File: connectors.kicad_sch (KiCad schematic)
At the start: 4 parts, among them J1 Conn_01x04_Pin, J2 Conn_01x04_Pin, J3 Conn_01x09_Pin, J4 Conn_02x03_Odd_Even

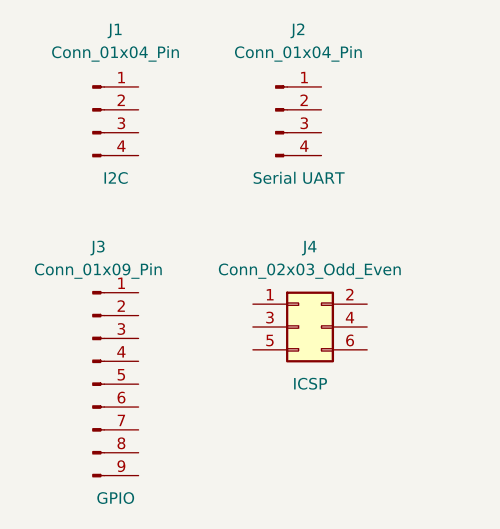
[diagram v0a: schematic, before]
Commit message: Arranged symbols.
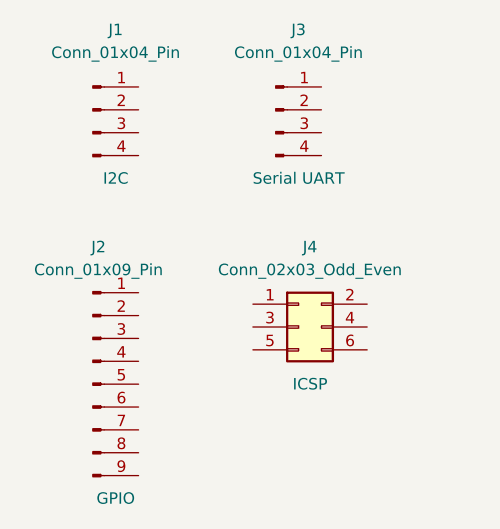
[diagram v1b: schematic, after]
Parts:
- renumbered J3 to J2, J2 to J3
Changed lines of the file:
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@@
 		(on_board yes)
 		(dnp no)
-		(property "Reference" "J3"
+		(property "Reference" "J2"
 			(at 93.345 87.63 0)
 			(effects
@@
 			(project ""
 				(path "/eb036d61-982e-41fc-ad07-0dff52d6a1cc/1c35631a-56f2-41a3-8845-0858340bff1a"
-					(reference "J3")
+					(reference "J2")
 					(unit 1)
 				)
@@
 		(on_board yes)
 		(dnp no)
-		(property "Reference" "J2"
+		(property "Reference" "J3"
 			(at 115.57 63.5 0)
 			(effects
@@
 			(project "MCU Datalogger"
 				(path "/eb036d61-982e-41fc-ad07-0dff52d6a1cc/1c35631a-56f2-41a3-8845-0858340bff1a"
-					(reference "J2")
+					(reference "J3")
 					(unit 1)
 				)

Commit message: Completed symbol-footprint associations.
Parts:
- J1, J3: footprint (none) -> Connector_PinHeader_2.54mm:PinHeader_1x04_P2.54mm_Vertical
- J2: footprint (none) -> Connector_PinHeader_2.54mm:PinHeader_1x09_P2.54mm_Vertical
- J4: footprint (none) -> Connector_PinHeader_2.54mm:PinHeader_2x03_P2.54mm_Vertical
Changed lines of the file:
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@@
 			)
 		)
-		(property "Footprint" ""
+		(property "Footprint" "Connector_PinHeader_2.54mm:PinHeader_2x03_P2.54mm_Vertical"
 			(at 115.57 96.52 0)
 			(effects
@@
 			)
 		)
-		(property "Footprint" ""
+		(property "Footprint" "Connector_PinHeader_2.54mm:PinHeader_1x09_P2.54mm_Vertical"
 			(at 92.71 102.87 0)
 			(effects
@@
 			)
 		)
-		(property "Footprint" ""
+		(property "Footprint" "Connector_PinHeader_2.54mm:PinHeader_1x04_P2.54mm_Vertical"
 			(at 113.03 72.39 0)
 			(effects
@@
 			)
 		)
-		(property "Footprint" ""
+		(property "Footprint" "Connector_PinHeader_2.54mm:PinHeader_1x04_P2.54mm_Vertical"
 			(at 92.71 72.39 0)
 			(effects

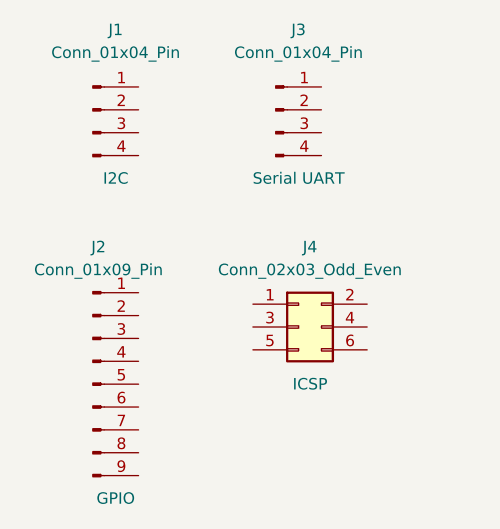
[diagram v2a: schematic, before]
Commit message: Completed wiring in the second sheet.
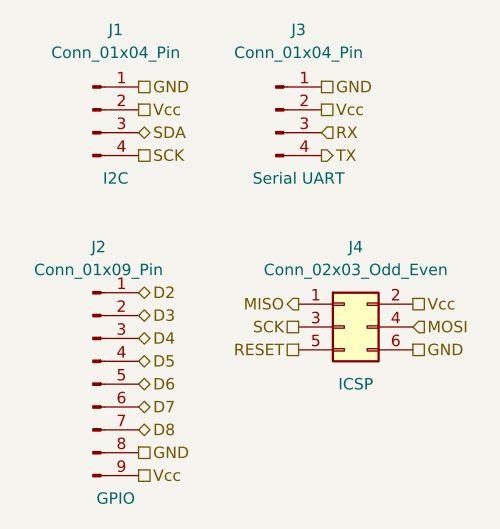
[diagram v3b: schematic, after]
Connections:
- net MISO: now reaches J4.1 (Pin_1)
- net Vcc: now reaches J4.2 (Pin_2)
- net Vcc: now also J1.2 (Pin_2), J2.9 (Pin_9), J3.2 (Pin_2)
- net SCK: now reaches J4.3 (Pin_3)
- net SCK: now also J1.4 (Pin_4)
- net MOSI: now reaches J4.4 (Pin_4)
- net RESET: now reaches J4.5 (Pin_5)
- net GND: now reaches J4.6 (Pin_6)
- net GND: now also J1.1 (Pin_1), J2.8 (Pin_8), J3.1 (Pin_1)
- net D2: now reaches J2.1 (Pin_1)
- net D3: now reaches J2.2 (Pin_2)
- net D4: now reaches J2.3 (Pin_3)
- net D5: now reaches J2.4 (Pin_4)
- net D6: now reaches J2.5 (Pin_5)
- net D7: now reaches J2.6 (Pin_6)
- net D8: now reaches J2.7 (Pin_7)
- net RX: now reaches J3.3 (Pin_3)
- net TX: now reaches J3.4 (Pin_4)
- net SDA: now reaches J1.3 (Pin_3)
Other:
- moved on the sheet: J4

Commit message: Fixed two defects in the schematic.
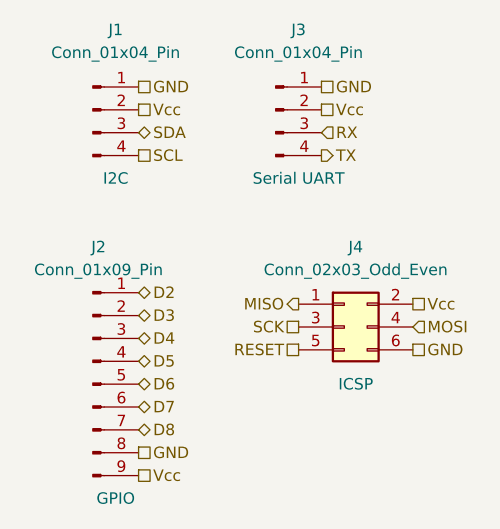
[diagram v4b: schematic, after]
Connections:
- net SCK: no longer J1.4 (Pin_4)
- new net SCL: J1.4 (Pin_4)
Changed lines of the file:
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@@
 	(generator_version "8.0")
 	(paper "A4")
-	(hierarchical_label "SCK"
+	(hierarchical_label "SCL"
 		(shape passive)
 		(at 97.79 77.47 0)
